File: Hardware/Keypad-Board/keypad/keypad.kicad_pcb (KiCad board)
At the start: 2 copper layers, 143 x 51 mm, 17 parts, among them J1 Conn_01x07, SW1 SW_Push_45deg, SW10 SW_Push_45deg, SW11 SW_Push_45deg, SW12 SW_Push_45deg, SW2 SW_Push_45deg, SW3 SW_Push_45deg, SW4 SW_Push_45deg, SW5 SW_Push_45deg, SW6 SW_Push_45deg, SW7 SW_Push_45deg, SW8 SW_Push_45deg, SW9 SW_Push_45deg

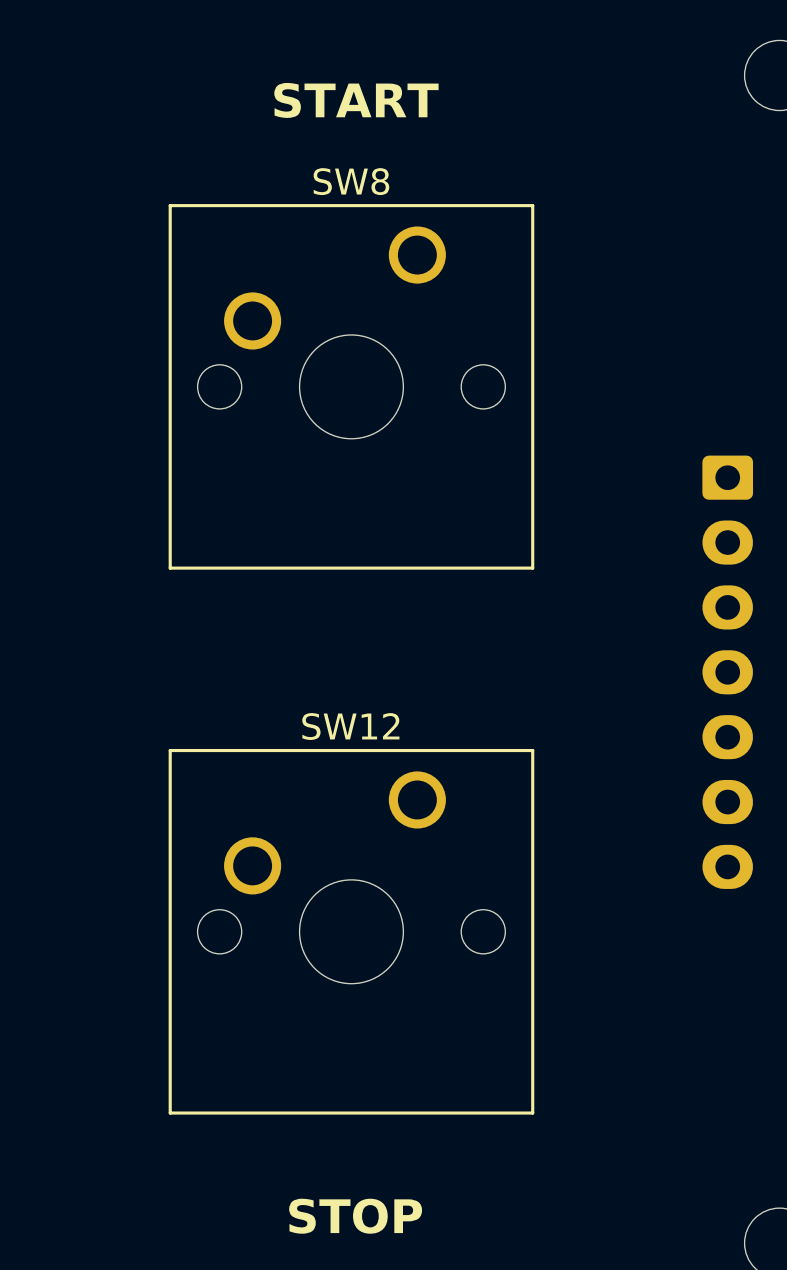
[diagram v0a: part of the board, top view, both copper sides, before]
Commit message: move start stop keys half a mm and then made fabrication outputs, fitment check good, ready for production
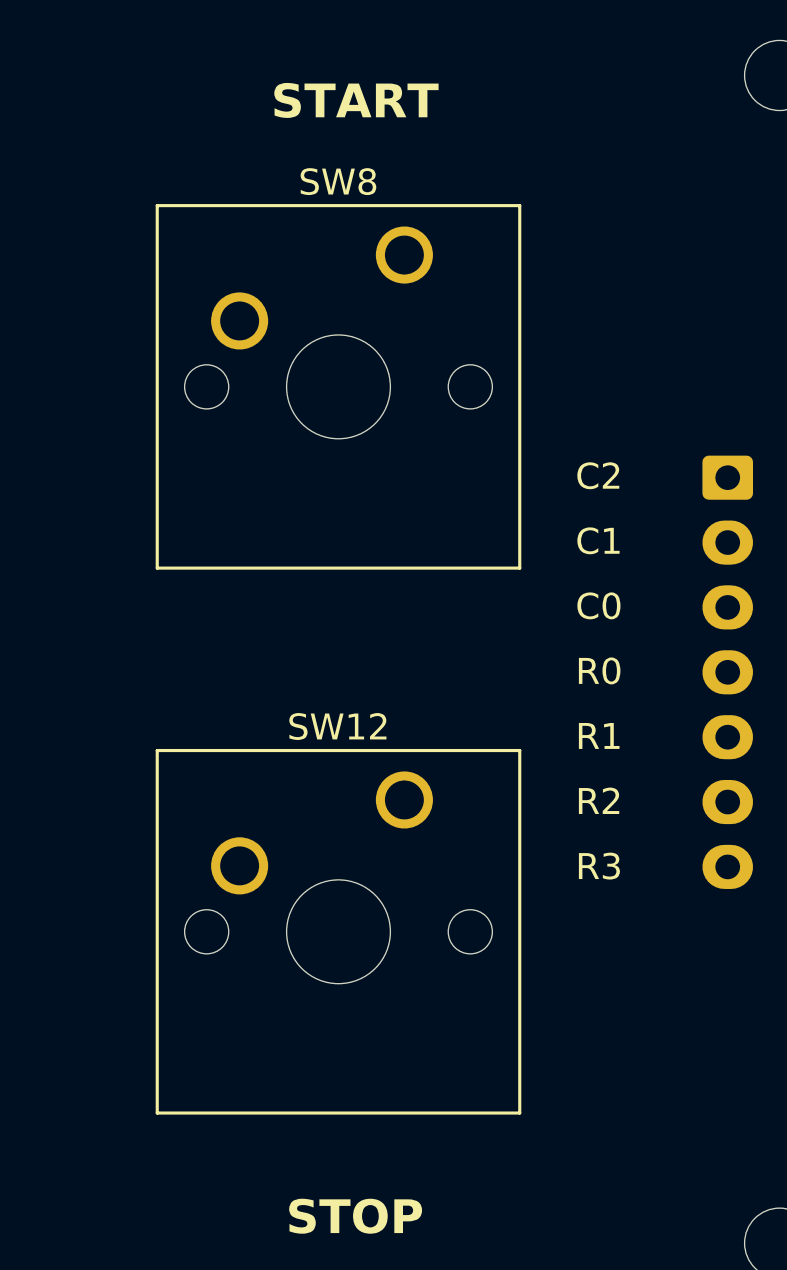
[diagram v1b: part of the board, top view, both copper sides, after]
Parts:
- moved SW12 0.50 mm to (239.5, 99.9)
- moved SW8 0.50 mm to (239.5, 78.9)
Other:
- board text added: "C0"
- board text added: "C1"
- board text added: "C2"
- board text added: "R0"
- board text added: "R1"
- board text added: "R2"
- board text added: "R3"
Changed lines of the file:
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@@
 		(locked yes)
 		(layer "F.Cu")
-		(at 240.04 99.92)
+		(at 239.54 99.92)
 		(descr "Cherry MX keyswitch, 1.00u, PCB mount, http://cherryamericas.com/wp-content/uploads/2014/12/mx_cat.pdf")
 		(tags "Cherry MX keyswitch 1.00u PCB")
@@
 		(locked yes)
 		(layer "F.Cu")
-		(at 240.04 78.92)
+		(at 239.54 78.92)
 		(descr "Cherry MX keyswitch, 1.00u, PCB mount, http://cherryamericas.com/wp-content/uploads/2014/12/mx_cat.pdf")
 		(tags "Cherry MX keyswitch 1.00u PCB")
@@
 		)
 	)
+	(gr_text "R3"
+		(at 247.043075 102.504865 0)
+		(layer "F.SilkS")
+		(effects
+			(font
+				(size 1 1)
+				(thickness 0.1)
+			)
+		)
+	)
 	(gr_text "9"
 		(at 213.790111 72.937656 0)
@@
 		)
 	)
+	(gr_text "R2"
+		(at 247.043075 99.997805 0)
+		(layer "F.SilkS")
+		(effects
+			(font
+				(size 1 1)
+				(thickness 0.1)
+			)
+		)
+	)
 	(gr_text "3"
 		(at 192.790111 115.937656 0)
@@
 		)
 	)
+	(gr_text "R0"
+		(at 247.043075 94.983686 0)
+		(layer "F.SilkS")
+		(effects
+			(font
+				(size 1 1)
+				(thickness 0.1)
+			)
+		)
+	)
 	(gr_text "5"
 		(at 129.790111 72.937656 0)
@@
 		)
 	)
+	(gr_text "C0"
+		(at 247.043075 92.476626 0)
+		(layer "F.SilkS")
+		(effects
+			(font
+				(size 1 1)
+				(thickness 0.1)
+			)
+		)
+	)
+	(gr_text "C2"
+		(at 247.043075 87.462507 0)
+		(layer "F.SilkS")
+		(effects
+			(font
+				(size 1 1)
+				(thickness 0.1)
+			)
+		)
+	)
+	(gr_text "C1"
+		(at 247.043075 89.969567 0)
+		(layer "F.SilkS")
+		(effects
+			(font
+				(size 1 1)
+				(thickness 0.1)
+			)
+		)
+	)
 	(gr_text "START"
 		(at 237.632373 73.009481 0)
@@
 		)
 	)
+	(gr_text "R1"
+		(at 247.043075 97.490746 0)
+		(layer "F.SilkS")
+		(effects
+			(font
+				(size 1 1)
+				(thickness 0.1)
+			)
+		)
+	)
 	(gr_text "STOP"
 		(at 237.632373 116.009481 0)
@@
 		)
 	)
+	(gr_text "R1"
+		(at 247.043075 97.414486 -0)
+		(layer "B.SilkS")
+		(effects
+			(font
+				(size 1 1)
+				(thickness 0.1)
+			)
+			(justify mirror)
+		)
+	)
+	(gr_text "C2"
+		(at 247.043075 87.386247 -0)
+		(layer "B.SilkS")
+		(effects
+			(font
+				(size 1 1)
+				(thickness 0.1)
+			)
+			(justify mirror)
+		)
+	)
+	(gr_text "C0"
+		(at 247.043075 92.400366 -0)
+		(layer "B.SilkS")
+		(effects
+			(font
+				(size 1 1)
+				(thickness 0.1)
+			)
+			(justify mirror)
+		)
+	)
+	(gr_text "R2"
+		(at 247.043075 99.921545 -0)
+		(layer "B.SilkS")
+		(effects
+			(font
+				(size 1 1)
+				(thickness 0.1)
+			)
+			(justify mirror)
+		)
+	)
+	(gr_text "R0"
+		(at 247.043075 94.907426 -0)
+		(layer "B.SilkS")
+		(effects
+			(font
+				(size 1 1)
+				(thickness 0.1)
+			)
+			(justify mirror)
+		)
+	)
+	(gr_text "C1"
+		(at 247.043075 89.893307 -0)
+		(layer "B.SilkS")
+		(effects
+			(font
+				(size 1 1)
+				(thickness 0.1)
+			)
+			(justify mirror)
+		)
+	)
+	(gr_text "R3"
+		(at 247.043075 102.428605 -0)
+		(layer "B.SilkS")
+		(effects
+			(font
+				(size 1 1)
+				(thickness 0.1)
+			)
+			(justify mirror)
+		)
+	)

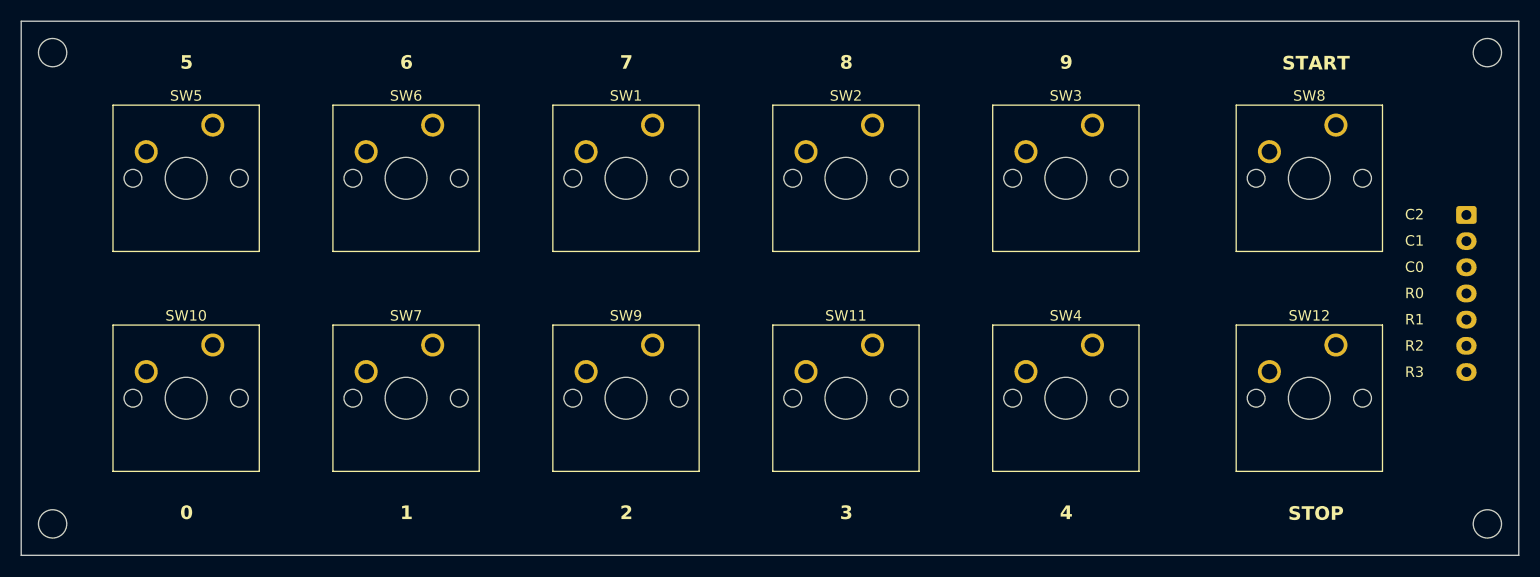
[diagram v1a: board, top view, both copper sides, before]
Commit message: almost forgot traces, route board and send to production
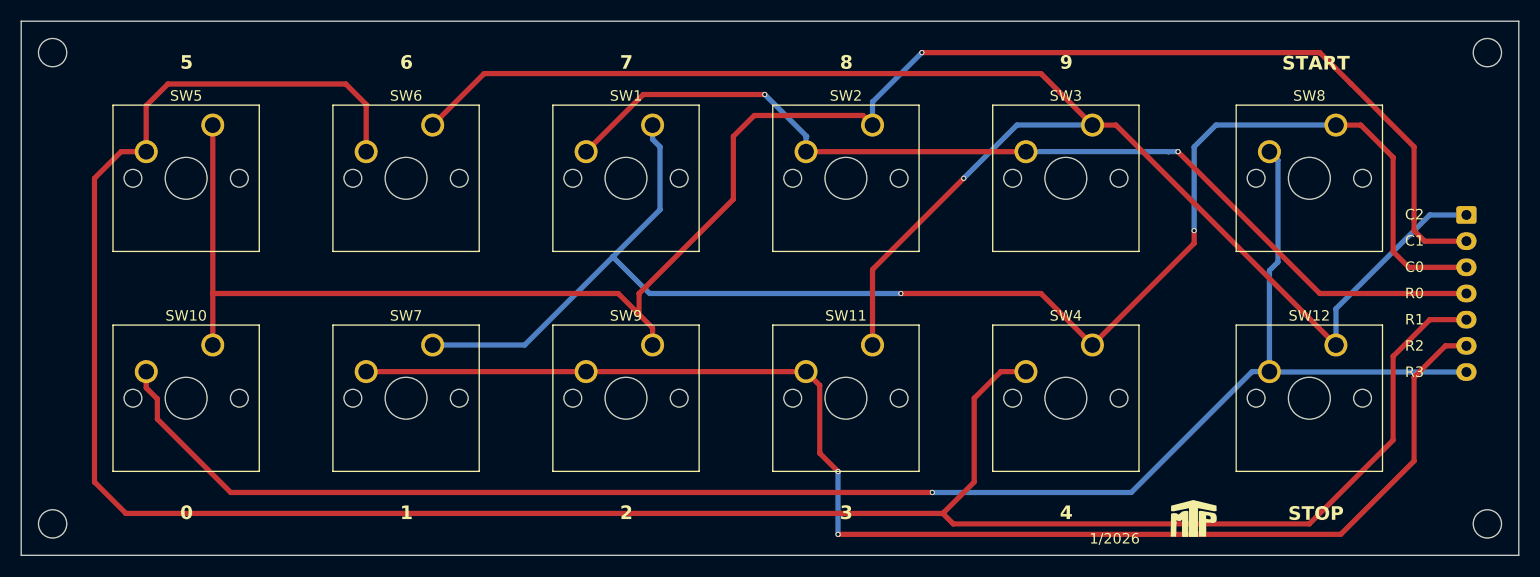
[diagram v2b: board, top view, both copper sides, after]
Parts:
- added REF**: MTP Logo 5mm Low Detail, Watermarks:MTP Logo 5mm Low Detail, F.Cu at (226.0, 117.0)
- added REF**: MTP Logo 10mm Low Detail, Watermarks:MTP Logo 10mm Low Detail, B.Cu at (187.5, 92.2)
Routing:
- net /Row_1: track 0.00 -> 230.3 mm
- net /Col_1: track 0.00 -> 174.2 mm, vias 0 -> 1
- net /Row_3: track 0.00 -> 159.3 mm, vias 0 -> 1
- net /Col_2: track 0.00 -> 152.6 mm, vias 0 -> 1
- net /Col_0: track 0.00 -> 145.4 mm, vias 0 -> 2
- net /Row_2: track 0.00 -> 130.9 mm, vias 0 -> 2
- net /Row_0: track 0.00 -> 95.1 mm, vias 0 -> 2
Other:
- board text added: "1/2026"
- board text added: "Keypad Board"
- board text added: "Michael Pate Version 2.0 01/2026"
